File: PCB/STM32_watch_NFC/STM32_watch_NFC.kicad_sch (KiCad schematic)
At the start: 39 parts, among them J1 Conn_01x06_Socket, Q1 BC817, SW1 SW_DPST_x2, SW2 SW_DPST_x2, SW3 SW_DPST_x2, U1 BH1750FVI-TR, U2 74AHCT1G125, U3 STM32L031G6Ux, Y1 32.768kHz

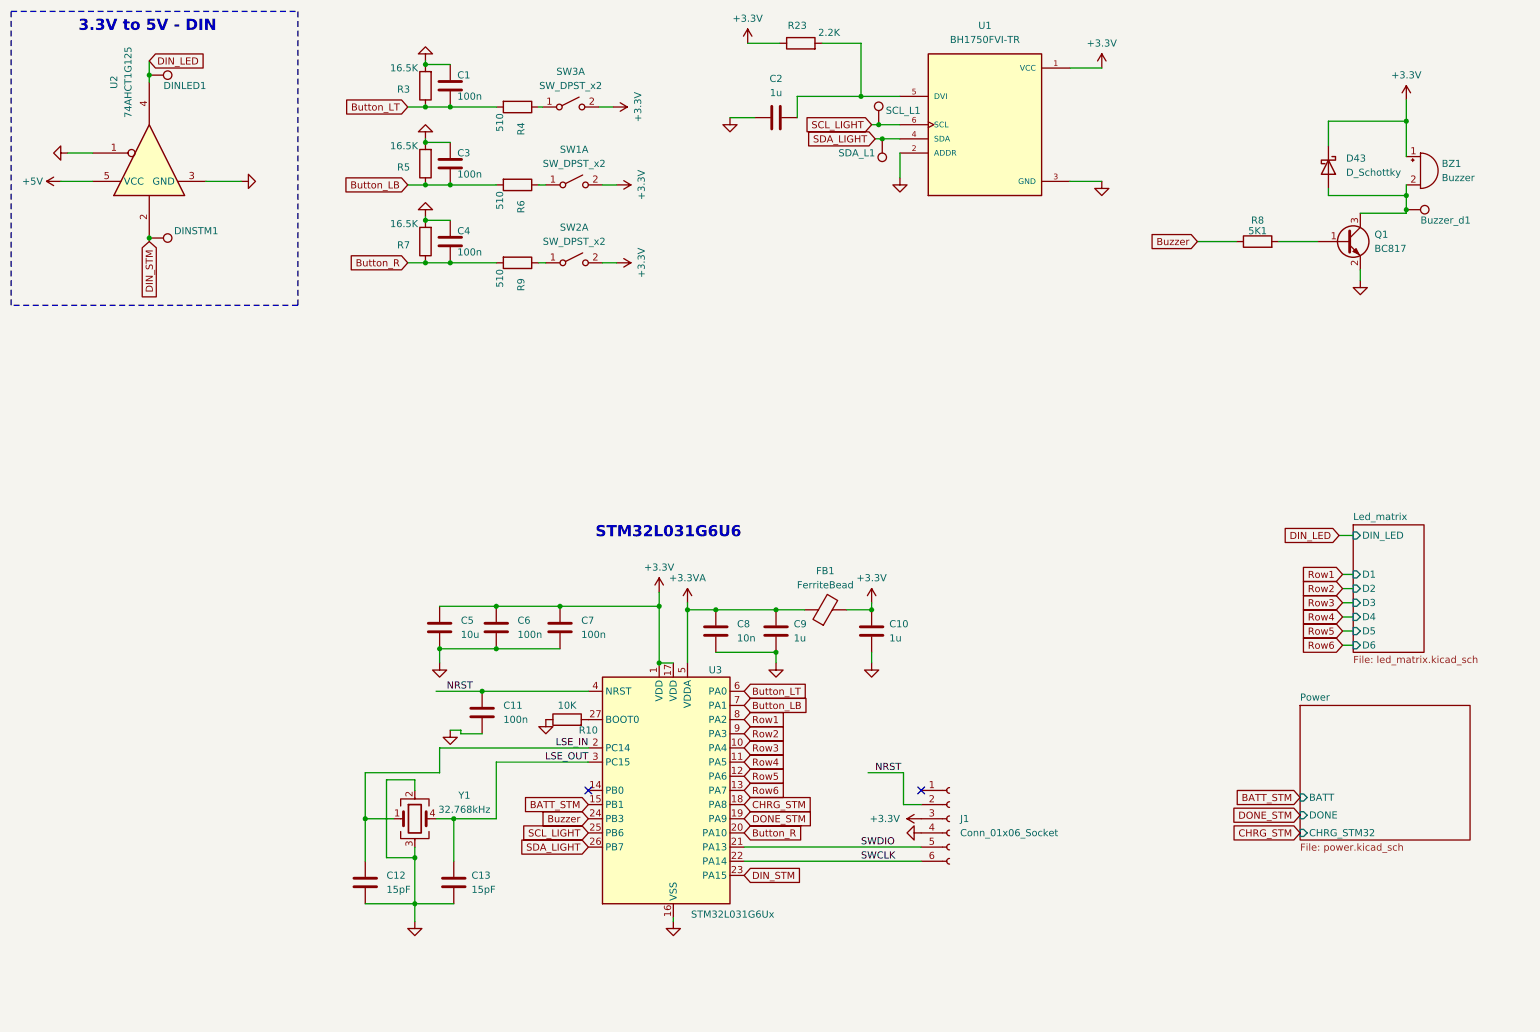
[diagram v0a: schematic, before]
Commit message: Whole power schema
I draw the whole power section and I am starting to create accelerometer with gyro
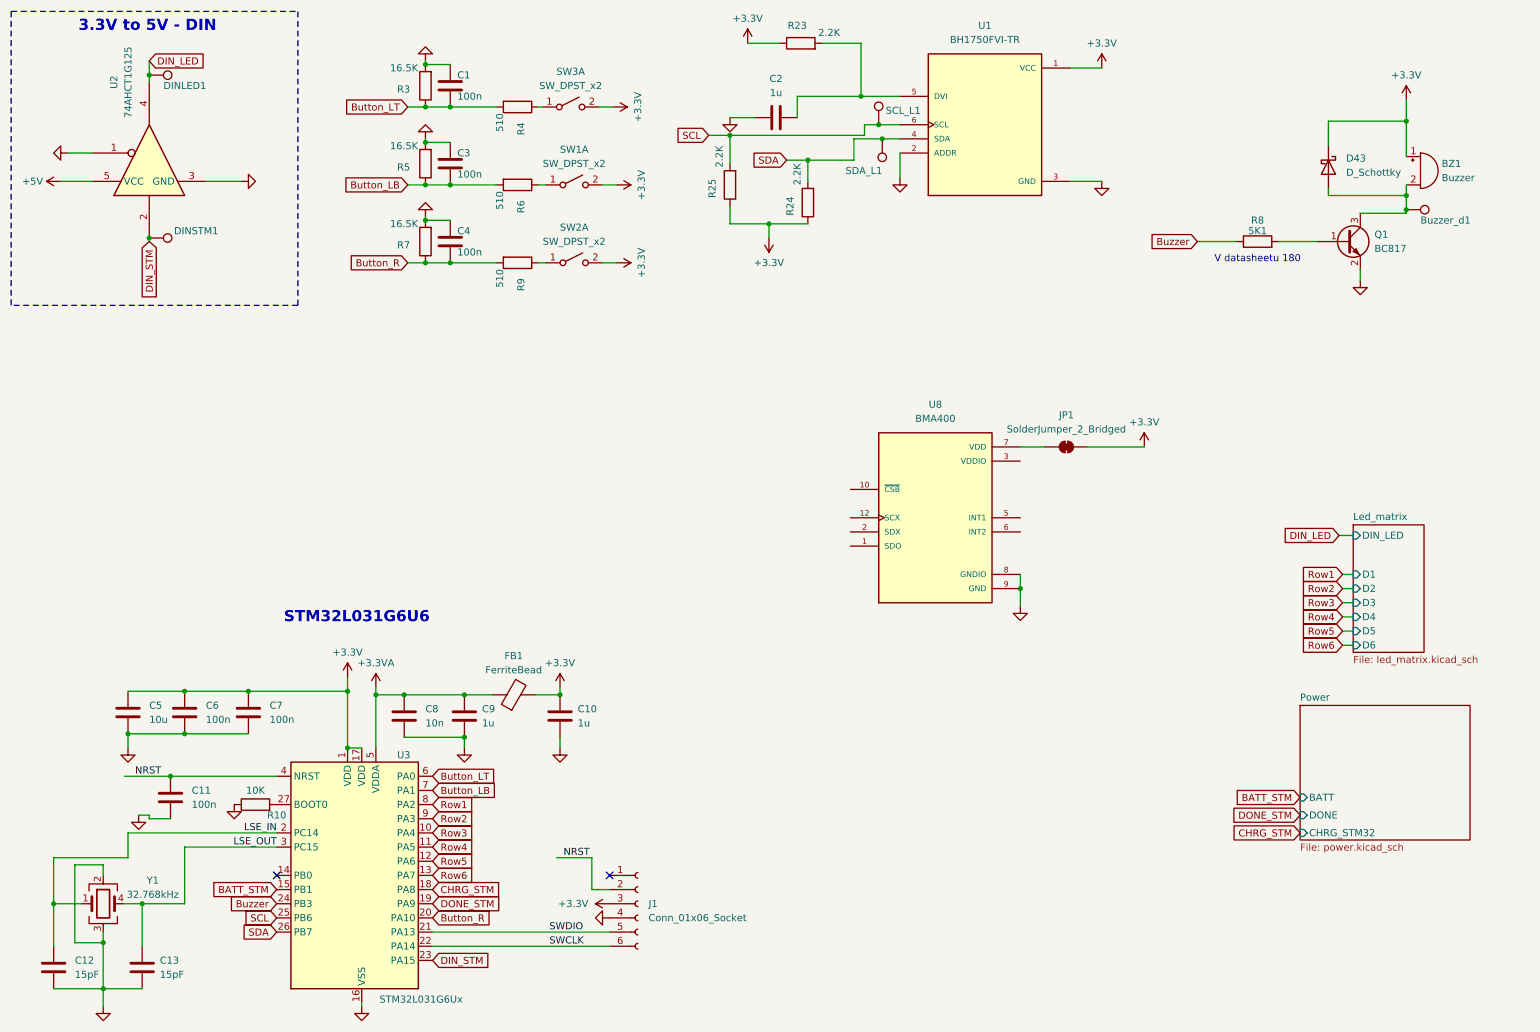
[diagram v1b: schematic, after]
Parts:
- added JP1: SolderJumper_2_Bridged, symbol Jumper:SolderJumper_2_Bridged
- added R24, R25: 2.2K, Resistor_SMD:R_0402_1005Metric, symbol Device:R
- added U8: BMA400, BMA400:XDCR_BMA400, symbol BMA400:BMA400
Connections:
- net +3.3V: now also JP1.2 (B), R24.1, R25.1
- net GND: now also U8.8 (GNDIO), U8.9 (GND)
- net SCL_LIGHT renamed SCL
- net SCL: now also R25.2
- net SDA_LIGHT renamed SDA
- net SDA: now also R24.2
- new net: JP1.1 (A), U8.7 (VDD)
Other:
- note added: "V datasheetu 180"
- moved on the sheet: C10, C11, C12, C13, C5, C6, C7, C8, C9, FB1, J1, R10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

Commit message: Schema done
I redraw some footprints and added accelerometer with gyro
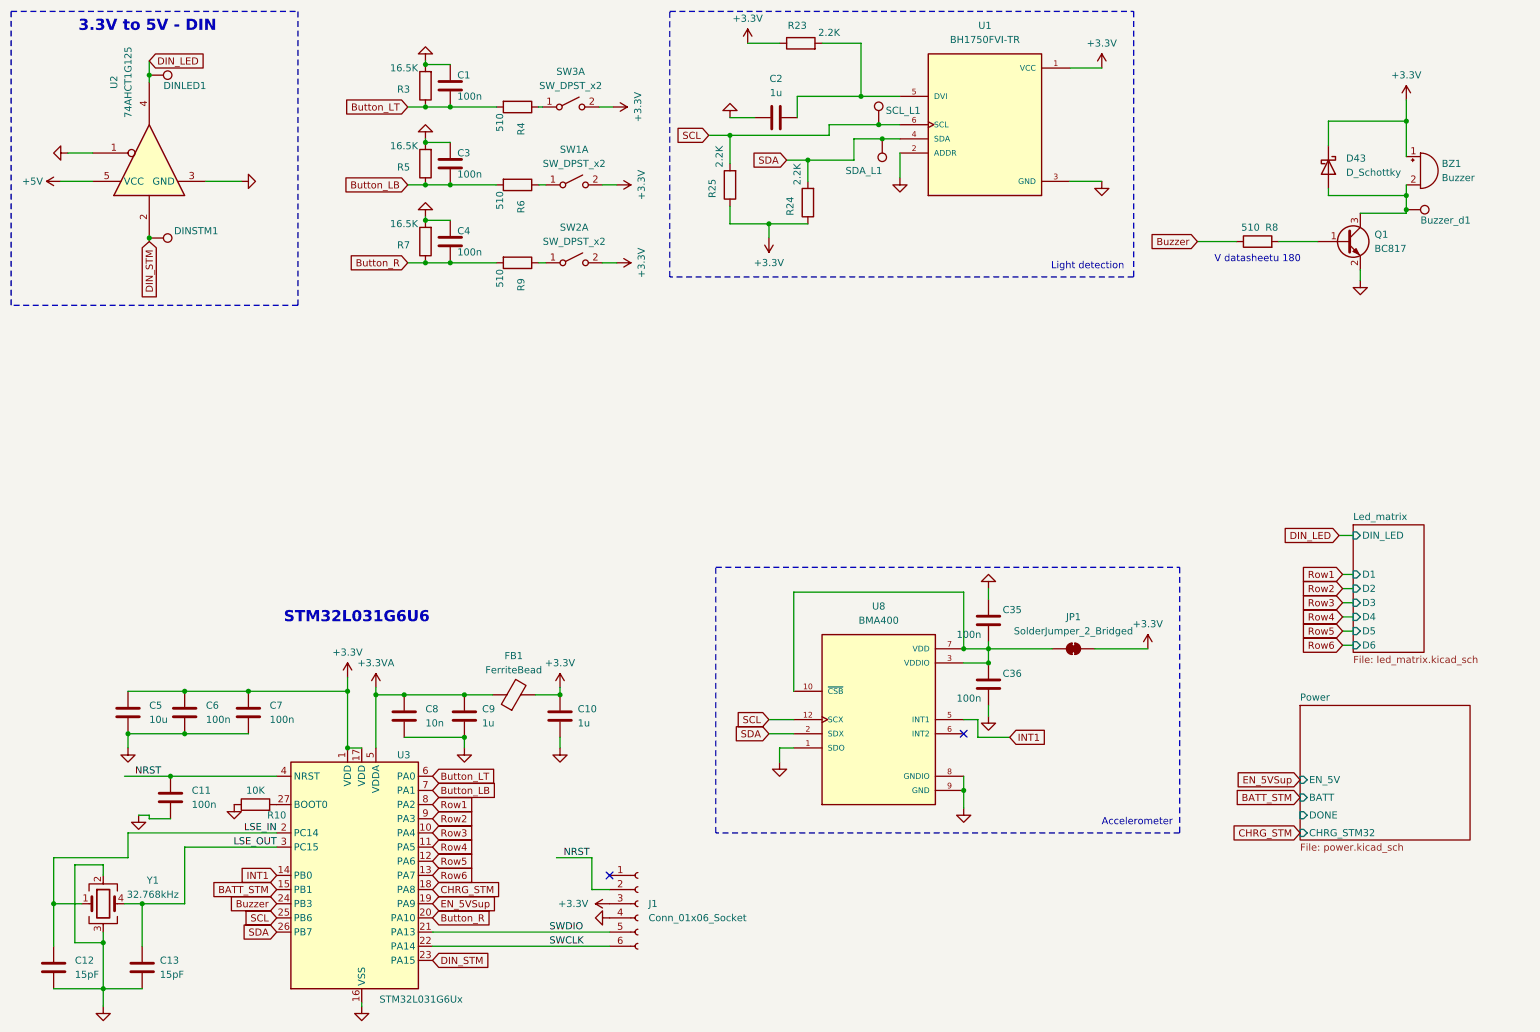
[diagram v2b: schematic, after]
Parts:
- added C35, C36: 100n, Capacitor_SMD:C_0201_0603Metric, symbol Device:C
- JP1: footprint (none) -> Jumper:SolderJumper-2_P1.3mm_Bridged_RoundedPad1.0x1.5mm
- R8: value 5K1 -> 510; LCSC C25905 -> C25123
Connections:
- net GND: now also U8.1 (SDO), C35.1, C36.2
- net SCL: now also U8.12 (SCX)
- net SDA: now also U8.2 (SDX)
- net at JP1.1 (A), U8.7 (VDD): now also U8.10 (~{CSB}), U8.3 (VDDIO), C35.2, C36.1
- net INT1: now reaches U3.14 (PB0)
- net INT1: now also U8.5 (INT1)
- net DONE_STM renamed EN_5VSup
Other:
- sheet Power ports: added EN_5V; removed none
- note added: "Accelerometer"
- note added: "Light detection"
- moved on the sheet: JP1, U8

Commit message: PCB rev.B.1 #2
every component has logical placement
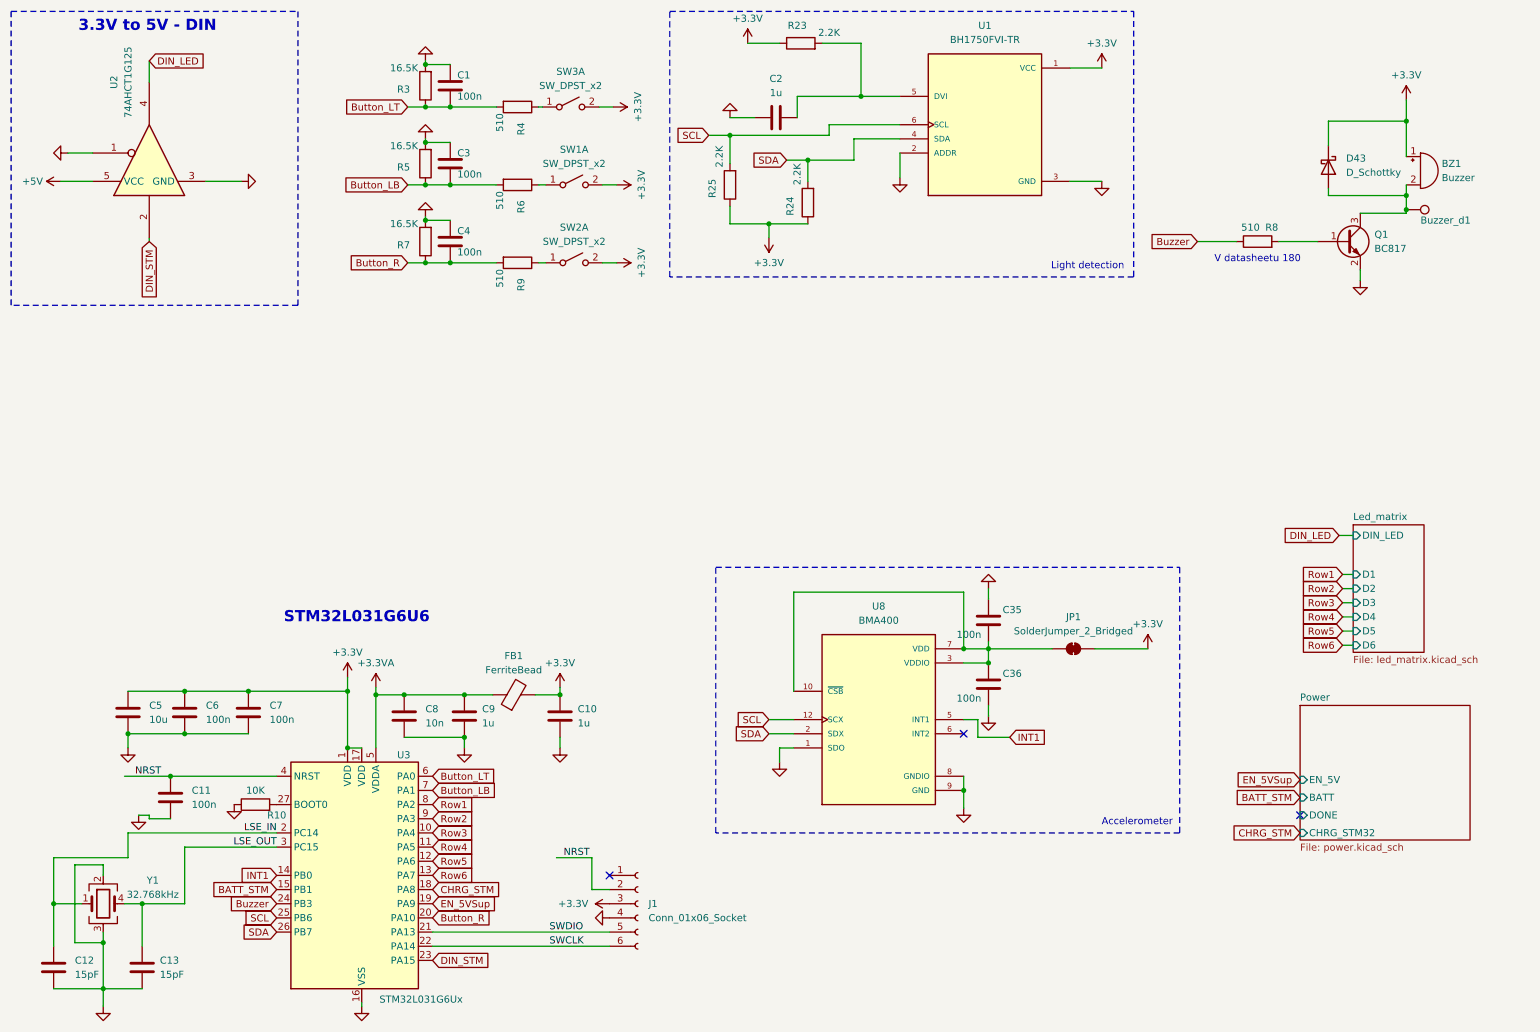
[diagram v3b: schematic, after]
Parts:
- removed DINLED1, DINSTM1, SCL_L1, SDA_L1: ~, TestPoint:TestPoint_Pad_D1.0mm, symbol Connector:TestPoint
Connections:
- no-connect marks 2 -> 3

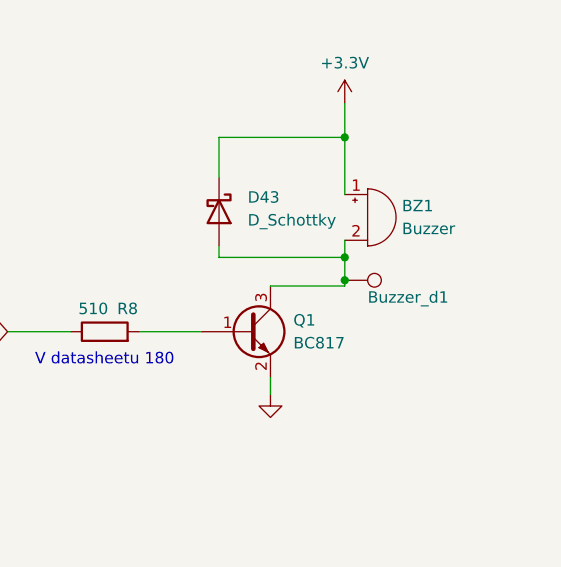
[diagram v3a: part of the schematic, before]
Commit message: PCB rev.B.1 #3
routing almost done - now checking and silkscreen
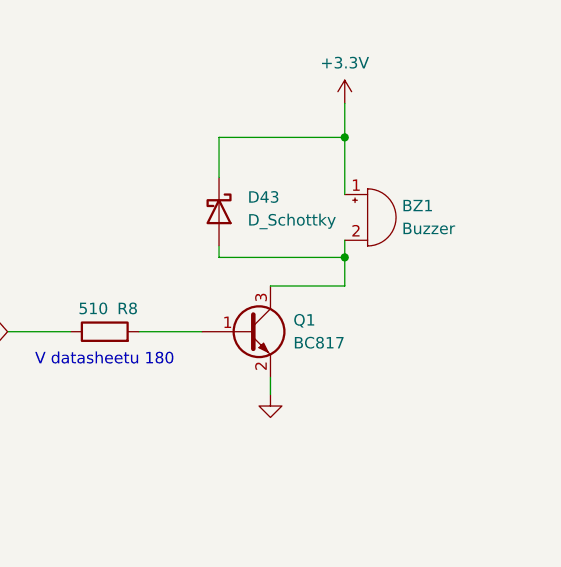
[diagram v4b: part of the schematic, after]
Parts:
- removed Buzzer_d1: ~, TestPoint:TestPoint_Pad_D1.0mm, symbol Connector:TestPoint
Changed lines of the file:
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@@
 	)
 	(junction
-		(at 262.255 47.625)
-		(diameter 0)
-		(color 0 0 0 0)
-	)
-	(junction
 		(at 86.36 57.15)
 		(diameter 0)
@@
 	(wire
 		(pts
-			(xy 262.255 45.085) (xy 262.255 47.625)
-		)
-		(stroke
-			(width 0)
-			(type default)
-		)
-	)
-	(wire
-		(pts
 			(xy 250.825 113.03) (xy 252.73 113.03)
 		)
@@
 	(wire
 		(pts
-			(xy 262.255 47.625) (xy 262.255 48.26)
+			(xy 262.255 45.085) (xy 262.255 48.26)
 		)
 		(stroke
@@
 					(unit 1)
 				)
-			)
-		)
-	)
-	(symbol
-		(lib_id "Connector:TestPoint")
-		(at 262.255 47.625 270)
-		(unit 1)
-		(exclude_from_sim no)
-		(in_bom yes)
-		(on_board yes)
-		(dnp no)
-		(property "Reference" "Buzzer_d1"
-			(at 264.795 49.53 90)
-			(effects
-				(font
-					(size 1.27 1.27)
-				)
-				(justify left)
-			)
-		)
-		(property "Value" "~"
-			(at 266.7 38.1 0)
-			(effects
-				(font
-					(size 1.27 1.27)
-				)
-				(justify left)
-			)
-		)
-		(property "Footprint" "TestPoint:TestPoint_Pad_D1.0mm"
-			(at 262.255 52.705 0)
-			(effects
-				(font
-					(size 1.27 1.27)
-				)
-				(hide yes)
-			)
-		)
-		(property "Datasheet" "~"
-			(at 262.255 52.705 0)
-			(effects
-				(font
-					(size 1.27 1.27)
-				)
-				(hide yes)
-			)
-		)
-		(property "Description" ""
-			(at 262.255 47.625 0)
-			(effects
-				(font
-					(size 1.27 1.27)
-				)
-				(hide yes)
-			)
-		)
-		(pin "1"
-		)
-		(instances
-			(project "STM32_watch_NFC"
-				(path "/e445874f-c7a3-43dd-b930-6bce1d4fa2ef"
-					(reference "Buzzer_d1")
-					(unit 1)
-				)

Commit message: rev.B.1
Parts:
- U2: LCSC C151417 -> C350557
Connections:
- no-connect marks 3 -> 2
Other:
- sheet Power ports: added none; removed DONE
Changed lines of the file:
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@@
 	)
 	(no_connect
-		(at 243.205 156.21)
-	)
-	(no_connect
 		(at 119.38 167.005)
 	)
@@
 			)
 		)
-		(property "LCSC" "C151417"
+		(property "LCSC" "C350557"
 			(at 36.83 37.465 0)
 			(effects
@@
 			)
 		)
-		(pin "DONE" input
-			(at 243.205 156.21 180)
-			(effects
-				(font
-					(size 1.27 1.27)
-				)
-				(justify left)
-			)
-		)
